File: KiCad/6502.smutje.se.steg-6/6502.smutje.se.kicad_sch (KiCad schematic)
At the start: 9 parts, among them U1 W65C02S, U2 LCD-016N002L

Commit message: Uppdatera steg-6 och steg-7 PNG:er med BE→+5V
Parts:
- added R5: (no value), symbol Device:R_US
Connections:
- net +5V: now also R5.1
- net Earth: no longer U1.36 (BE)
- new net: R5.2, U1.36 (BE)
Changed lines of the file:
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@@
-	(wire
-		(pts
-			(xy 80.01 66.04) (xy 80.01 68.58)
-		)
-		(stroke
-			(width 0)
-			(type default)
-		)
-	)
 	(wire
 		(pts
@@
 	(wire
 		(pts
+			(xy 62.23 63.5) (xy 62.23 66.04)
+		)
+		(stroke
+			(width 0)
+			(type default)
+		)
+	)
+	(wire
+		(pts
 			(xy 71.12 50.8) (xy 71.12 53.34)
 		)
@@
 	(wire
 		(pts
+			(xy 62.23 66.04) (xy 85.09 66.04)
+		)
+		(stroke
+			(width 0)
+			(type default)
+		)
+	)
+	(wire
+		(pts
 			(xy 105.41 66.04) (xy 116.84 66.04)
 		)
@@
 		(pts
 			(xy 163.83 96.52) (xy 173.99 96.52)
-		)
-		(stroke
-			(width 0)
-			(type default)
-		)
-	)
-	(wire
-		(pts
-			(xy 85.09 66.04) (xy 80.01 66.04)
 		)
 		(stroke
@@
 	(symbol
 		(lib_id "power:Earth")
-		(at 80.01 68.58 0)
-		(unit 1)
-		(body_style 1)
-		(exclude_from_sim no)
-		(in_bom yes)
-		(on_board yes)
-		(in_pos_files yes)
-		(dnp no)
-		(fields_autoplaced yes)
-		(property "Reference" "#PWR08"
-			(at 80.01 74.93 0)
-			(hide yes)
-			(show_name no)
-			(do_not_autoplace no)
-			(effects
-				(font
-					(size 1.27 1.27)
-				)
-			)
-		)
-		(property "Value" "Earth"
-			(at 80.01 73.66 0)
-			(hide yes)
-			(show_name no)
-			(do_not_autoplace no)
-			(effects
-				(font
-					(size 1.27 1.27)
-				)
-			)
-		)
-		(property "Footprint" ""
-			(at 80.01 68.58 0)
-			(hide yes)
-			(show_name no)
-			(do_not_autoplace no)
-			(effects
-				(font
-					(size 1.27 1.27)
-				)
-			)
-		)
-		(property "Datasheet" ""
-			(at 80.01 68.58 0)
-			(hide yes)
-			(show_name no)
-			(do_not_autoplace no)
-			(effects
-				(font
-					(size 1.27 1.27)
-				)
-			)
-		)
-		(property "Description" "Power symbol creates a global label with name \"Earth\""
-			(at 80.01 68.58 0)
-			(hide yes)
-			(show_name no)
-			(do_not_autoplace no)
-			(effects
-				(font
-					(size 1.27 1.27)
-				)
-			)
-		)
-		(pin "1"
-		)
-		(instances
-			(project "6502.smutje.se"
-				(path "/6aa7970e-7944-4a13-90e7-04df56da4812"
-					(reference "#PWR08")
-					(unit 1)
-				)
-			)
-		)
-	)
-	(symbol
-		(lib_id "power:Earth")
 		(at 184.15 101.6 0)
 		(unit 1)
@@
 	)
 	(symbol
+		(lib_id "power:+5V")
+		(at 62.23 55.88 0)
+		(unit 1)
+		(body_style 1)
+		(exclude_from_sim no)
+		(in_bom yes)
+		(on_board yes)
+		(in_pos_files yes)
+		(dnp no)
+		(fields_autoplaced yes)
+		(property "Reference" "#PWR08"
+			(at 62.23 59.69 0)
+			(hide yes)
+			(show_name no)
+			(do_not_autoplace no)
+			(effects
+				(font
+					(size 1.27 1.27)
+				)
+			)
+		)
+		(property "Value" "+5V"
+			(at 62.23 50.8 0)
+			(show_name no)
+			(do_not_autoplace no)
+			(effects
+				(font
+					(size 1.27 1.27)
+				)
+			)
+		)
+		(property "Footprint" ""
+			(at 62.23 55.88 0)
+			(hide yes)
+			(show_name no)
+			(do_not_autoplace no)
+			(effects
+				(font
+					(size 1.27 1.27)
+				)
+			)
+		)
+		(property "Datasheet" ""
+			(at 62.23 55.88 0)
+			(hide yes)
+			(show_name no)
+			(do_not_autoplace no)
+			(effects
+				(font
+					(size 1.27 1.27)
+				)
+			)
+		)
+		(property "Description" "Power symbol creates a global label with name \"+5V\""
+			(at 62.23 55.88 0)
+			(hide yes)
+			(show_name no)
+			(do_not_autoplace no)
+			(effects
+				(font
+					(size 1.27 1.27)
+				)
+			)
+		)
+		(pin "1"
+		)
+		(instances
+			(project "6502.smutje.se"
+				(path "/6aa7970e-7944-4a13-90e7-04df56da4812"
+					(reference "#PWR08")
+					(unit 1)
+				)
+			)
+		)
+	)
+	(symbol
 		(lib_id "power:Earth")
 		(at 166.37 71.12 0)
@@
 					(unit 1)
 				)
+			)
+		)
+	)
+	(symbol
+		(lib_id "Device:R_US")
+		(at 62.23 59.69 0)
+		(unit 1)
+		(body_style 1)
+		(exclude_from_sim no)
+		(in_bom yes)
+		(on_board yes)
+		(in_pos_files yes)
+		(dnp no)
+		(property "Reference" "R5"
+			(at 64.77 58.4199 90)
+			(show_name no)
+			(do_not_autoplace no)
+			(effects
+				(font
+					(size 1.27 1.27)
+				)
+				(justify left)
+			)
+		)
+		(property "Value" ""
+			(at 64.77 60.9599 0)
+			(show_name no)
+			(do_not_autoplace no)
+			(effects
+				(font
+					(size 1.27 1.27)
+				)
+				(justify left)
+			)
+		)
+		(property "Footprint" ""
+			(at 63.246 59.944 90)
+			(hide yes)
+			(show_name no)
+			(do_not_autoplace no)
+			(effects
+				(font
+					(size 1.27 1.27)
+				)
+			)
+		)
+		(property "Datasheet" ""
+			(at 62.23 59.69 0)
+			(hide yes)
+			(show_name no)
+			(do_not_autoplace no)
+			(effects
+				(font
+					(size 1.27 1.27)
+				)
+			)
+		)
+		(property "Description" "Resistor, US symbol"
+			(at 62.23 59.69 0)
+			(hide yes)
+			(show_name no)
+			(do_not_autoplace no)
+			(effects
+				(font
+					(size 1.27 1.27)
+				)
+			)
+		)
+		(pin "1"
+		)
+		(pin "2"
+		)
+		(instances
+			(project "6502.smutje.se"
+				(path "/6aa7970e-7944-4a13-90e7-04df56da4812"
+					(reference "R5")
+					(unit 1)
+				)

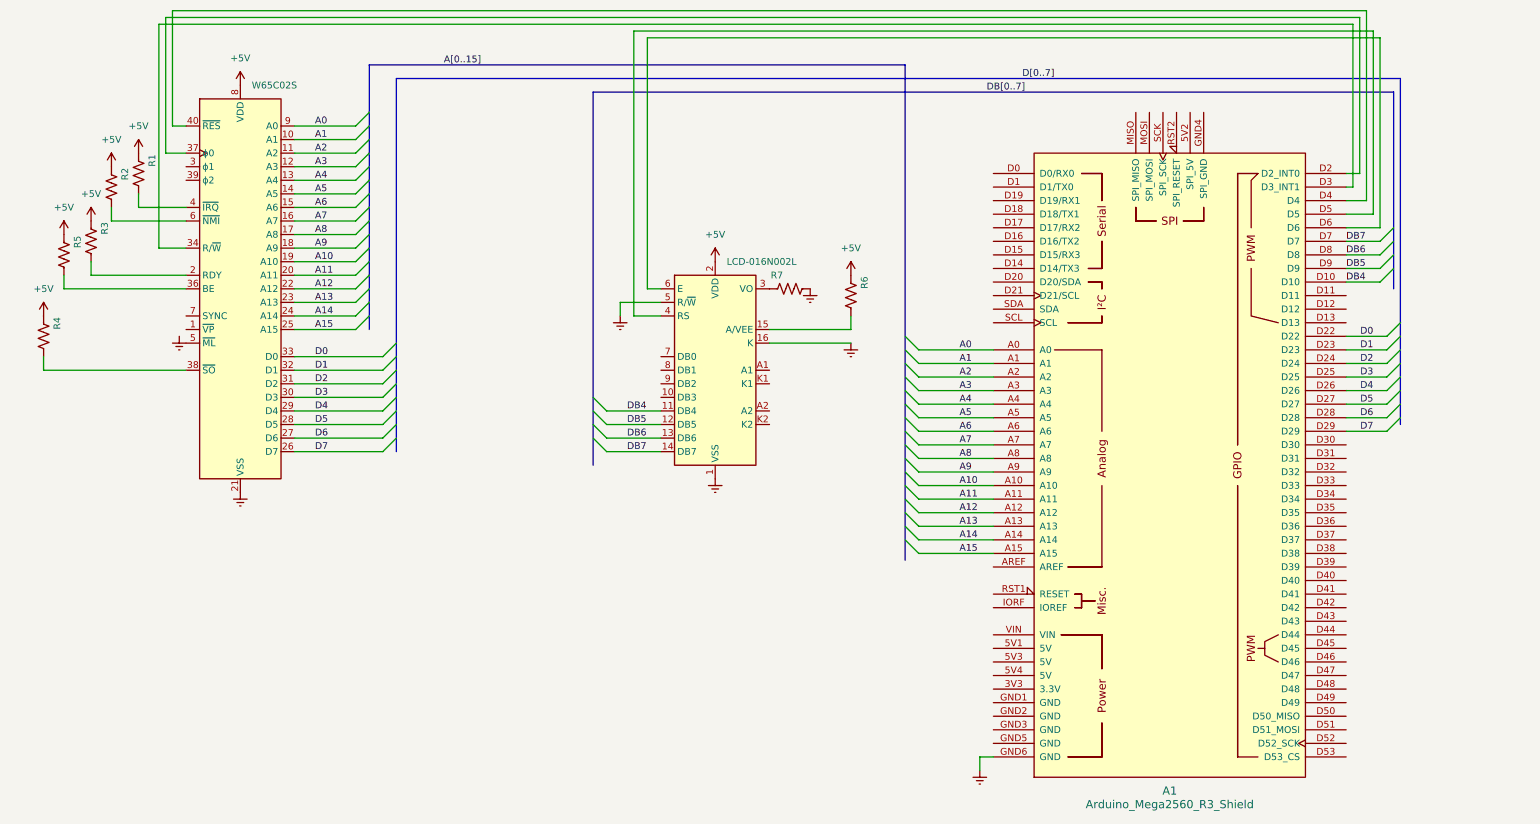
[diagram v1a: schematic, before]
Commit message: Steg 6 & 7: knappar + SYNC tillagda, nya PNG:er
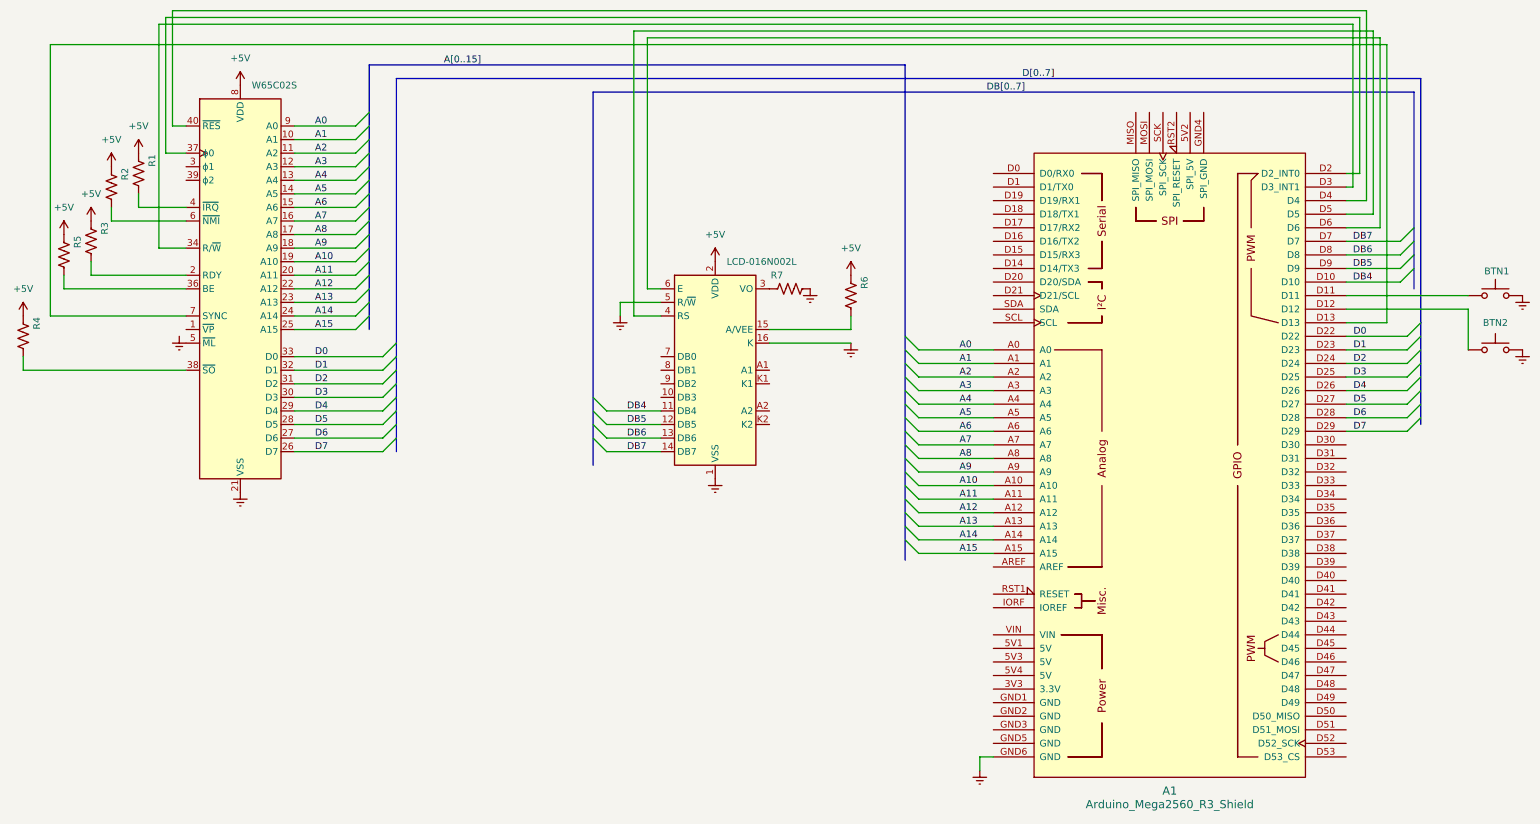
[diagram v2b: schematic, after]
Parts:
- added BTN1, BTN2: SW_Push, symbol Switch:SW_Push
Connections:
- net Earth: now also BTN1.2, BTN2.2
- net at A1.D11: now also BTN1.1
- net at A1.D12: now also BTN2.1
- net at A1.D13: now also U1.7 (SYNC)
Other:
- moved on the sheet: R4
